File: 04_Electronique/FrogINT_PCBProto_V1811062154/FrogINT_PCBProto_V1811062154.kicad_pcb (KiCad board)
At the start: 2 copper layers, 75.8 x 75.8 mm, 38 parts, among them IC1 TTP223-BA6, J1 USB_B_Mini, J2 Conn_01x01_Female, J3 AVR-JTAG-10, Q1 PMV48XP, Q2 PMV48XP, U1 NCP1117-5.0_SOT223, U2 LP2985-3.3, U3 ATmega16U4RC-AU, Y1 16MHz

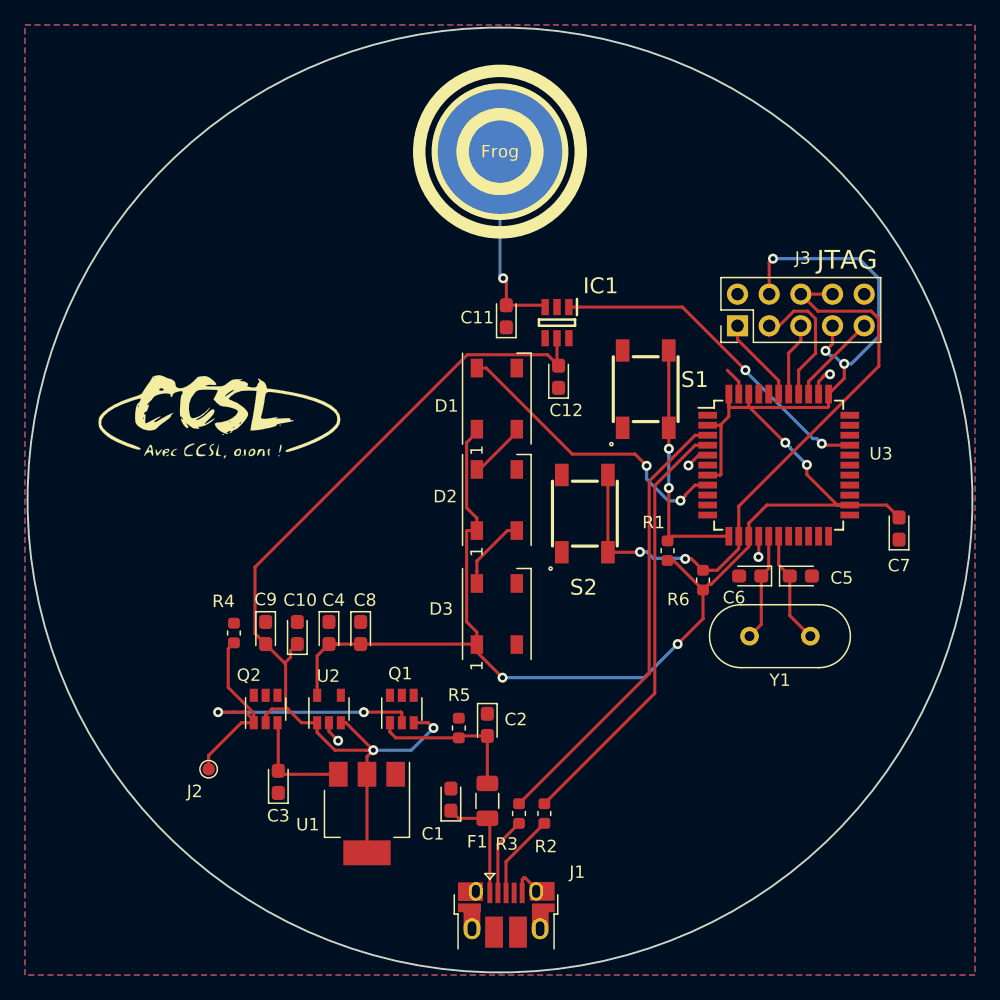
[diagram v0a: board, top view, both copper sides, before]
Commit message: Commit du 05/02/2019 :
Création d'une nouvelle forme de PCB,
Placement sommaire des composants,
Utilisation de Freerouting.jar pour effectuer une partie du routage.
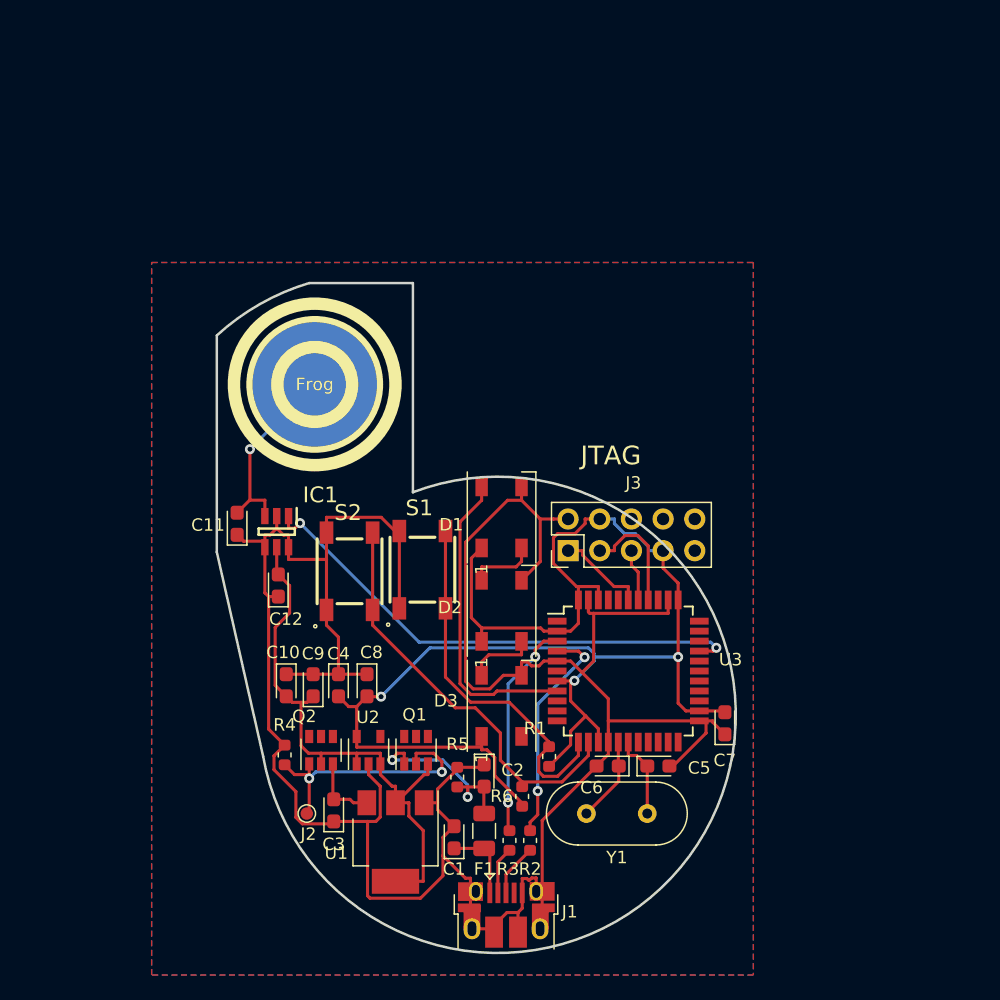
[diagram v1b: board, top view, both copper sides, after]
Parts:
- removed G***: LOGO, FTA_FrogINT_Library_Footprint_Package:Logo_CCSL_Silk
- removed G***: LOGO, FTA_FrogINT_Library_Footprint_Package:Logo_CCSL_Silk_Bottom
- removed G***: LOGO, FTA_FrogINT_Library_Footprint_Package:Logo_Thales_Silk_Bottom
- moved IC1 28.0 mm to (124.8, 100.8)
- moved C12 28.0 mm to (125.0, 105.2)
- moved C11 27.3 mm to (121.7, 100.2)
- moved TS1 23.9 mm to (127.9, 89.0)
- moved S1 23.0 mm to (136.5, 103.9)
- moved R6 22.6 mm to (144.5, 122.1)
- moved J3 22.6 mm to (148.2, 102.4)
- moved C7 21.0 mm to (160.8, 116.2)
- moved U3 20.4 mm to (153.0, 112.0)
- moved S2 19.4 mm to (130.7, 104.0)
- moved Y1 19.3 mm to (154.6, 123.4)
- moved C6 19.1 mm to (151.4, 119.6)
- moved C5 19.0 mm to (155.4, 119.6)
- moved R1 19.0 mm to (146.7, 118.9)
- moved R4 10.6 mm to (125.5, 118.7)
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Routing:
- net GND: track 12.6 -> 217.9 mm, vias 4 -> 0
- net +5V: track 79.0 -> 46.5 mm, vias 2 -> 0
- net +3V3: track 142.6 -> 120.1 mm, vias 7 -> 3
- net /D-: track 36.4 -> 17.5 mm, vias 0 -> 2
- net /reset: track 50.7 -> 33.5 mm, vias 2 -> 0
- net /D+: track 34.8 -> 18.1 mm, vias 0 -> 2
- net /Input_Int_Touch: track 27.2 -> 41.1 mm
- net /Vin: track 32.1 -> 21.2 mm
- net /Input_Interrupt: track 20.4 -> 30.0 mm, vias 2 -> 0
- net Net-(J3-Pad9): track 7.32 -> 0.00 mm
- net Net-(C3-Pad2): track 8.81 -> 5.63 mm
- net Net-(C1-Pad1): track 9.24 -> 6.17 mm
- net Net-(J3-Pad3): track 12.2 -> 9.29 mm
- net Net-(J1-Pad3): track 6.85 -> 4.22 mm
- net Net-(J1-Pad2): track 6.28 -> 3.80 mm
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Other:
- board size 75.8 x 75.8 mm -> 41.6 x 53.7 mm

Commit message: 12/02/2019 : Remplacement des gros boutons par des plus petits
Impact :
	Mise à jour du fichier Excel FrogINT_BOM_V03-Commit-22-01-2019_RFQ_RS.xlsx suite à la mise à jour de la BOM (Attention pour les chiffrage en cours)
	Création des fichiers sources mécaniques pour ce nouveau Switch_PTS810SJG250SMTRLFS
	Mise à jour des références des librairies (pointeur).
	Déplacement partiel de la librairie SamacSys_Parts directement dans la "racine" du projet (et non plus dans l'arborescence C: etc.)
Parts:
- S1, S2: value SKQGAKE010 -> PTS810SJG250SMTRLFS; footprint SamacSys_Parts:SKQGAKE010 -> SamacSys_Parts:PTS810SJG250SMTRLFS
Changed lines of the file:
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@@
   (page A4)
   (layers
-    (0 F.Cu signal)
-    (31 B.Cu signal)
+    (0 F.Cu signal hide)
+    (31 B.Cu signal hide)
     (32 B.Adhes user)
     (33 F.Adhes user)
@@
     (add_net /Cap-TouchSensor)
   )
+  (module SamacSys_Parts:PTS810SJG250SMTRLFS (layer F.Cu)
+    (at 136.525 103.886 90)
+    (descr pts810)
+    (tags Switch)
+    (attr smd)
+    (fp_text reference S1 (at -0.25 0 90) (layer F.SilkS)
+      (effects (font (size 1.27 1.27) (thickness 0.254)))
+    )
+    (fp_text value PTS810SJG250SMTRLFS (at -0.25 0 90) (layer F.SilkS) hide
+      (effects (font (size 1.27 1.27) (thickness 0.254)))
+    )
+    (fp_arc (start -3 -1.1) (end -3 -1) (angle 180) (layer F.SilkS) (width 0.2))
+    (fp_arc (start -3 -1.1) (end -3 -1.2) (angle 180) (layer F.SilkS) (width 0.2))
+    (fp_line (start -3 -1) (end -3 -1) (layer F.SilkS) (width 0.2))
+    (fp_line (start -3 -1.2) (end -3 -1.2) (layer F.SilkS) (width 0.2))
+    (fp_line (start -2.1 1.6) (end 2.075 1.6) (layer F.SilkS) (width 0.1))
+    (fp_line (start -2.1 -1.6) (end 2.075 -1.6) (layer F.SilkS) (width 0.1))
+    (fp_line (start -4.1 2.6) (end -4.1 -2.6) (layer Dwgs.User) (width 0.1))
+    (fp_line (start 3.6 2.6) (end -4.1 2.6) (layer Dwgs.User) (width 0.1))
+    (fp_line (start 3.6 -2.6) (end 3.6 2.6) (layer Dwgs.User) (width 0.1))
+    (fp_line (start -4.1 -2.6) (end 3.6 -2.6) (layer Dwgs.User) (width 0.1))
+    (fp_line (start -2.1 1.6) (end -2.1 -1.6) (layer Dwgs.User) (width 0.2))
+    (fp_line (start 2.1 1.6) (end -2.1 1.6) (layer Dwgs.User) (width 0.2))
+    (fp_line (start 2.1 -1.6) (end 2.1 1.6) (layer Dwgs.User) (width 0.2))
+    (fp_line (start -2.1 -1.6) (end 2.1 -1.6) (layer Dwgs.User) (width 0.2))
+    (pad 4 smd rect (at 2.075 1.075 180) (size 0.65 1.05) (layers F.Cu F.Paste F.Mask)
+      (net 22 /Input_Interrupt))
+    (pad 3 smd rect (at -2.075 1.075 180) (size 0.65 1.05) (layers F.Cu F.Paste F.Mask)
+      (net 22 /Input_Interrupt))
+    (pad 2 smd rect (at 2.075 -1.075 180) (size 0.65 1.05) (layers F.Cu F.Paste F.Mask)
+      (net 1 GND))
+    (pad 1 smd rect (at -2.075 -1.075 180) (size 0.65 1.05) (layers F.Cu F.Paste F.Mask)
+      (net 1 GND))
+    (model ${KIPRJMOD}/Library/PTS810SJG250SMTRLFS.step
+      (at (xyz 0 0 0))
+      (scale (xyz 1 1 1))
+      (rotate (xyz 0 0 0))
+    )
+  )
+  (module SamacSys_Parts:PTS810SJG250SMTRLFS (layer F.Cu)
+    (at 130.683 104.013 90)
+    (descr pts810)
+    (tags Switch)
+    (attr smd)
+    (fp_text reference S2 (at -0.25 0 90) (layer F.SilkS)
+      (effects (font (size 1.27 1.27) (thickness 0.254)))
+    )
+    (fp_text value PTS810SJG250SMTRLFS (at -0.25 0 90) (layer F.SilkS) hide
+      (effects (font (size 1.27 1.27) (thickness 0.254)))
+    )
+    (fp_line (start -2.1 -1.6) (end 2.1 -1.6) (layer Dwgs.User) (width 0.2))
+    (fp_line (start 2.1 -1.6) (end 2.1 1.6) (layer Dwgs.User) (width 0.2))
+    (fp_line (start 2.1 1.6) (end -2.1 1.6) (layer Dwgs.User) (width 0.2))
+    (fp_line (start -2.1 1.6) (end -2.1 -1.6) (layer Dwgs.User) (width 0.2))
+    (fp_line (start -4.1 -2.6) (end 3.6 -2.6) (layer Dwgs.User) (width 0.1))
+    (fp_line (start 3.6 -2.6) (end 3.6 2.6) (layer Dwgs.User) (width 0.1))
+    (fp_line (start 3.6 2.6) (end -4.1 2.6) (layer Dwgs.User) (width 0.1))
+    (fp_line (start -4.1 2.6) (end -4.1 -2.6) (layer Dwgs.User) (width 0.1))
+    (fp_line (start -2.1 -1.6) (end 2.075 -1.6) (layer F.SilkS) (width 0.1))
+    (fp_line (start -2.1 1.6) (end 2.075 1.6) (layer F.SilkS) (width 0.1))
+    (fp_line (start -3 -1.2) (end -3 -1.2) (layer F.SilkS) (width 0.2))
+    (fp_line (start -3 -1) (end -3 -1) (layer F.SilkS) (width 0.2))
+    (fp_arc (start -3 -1.1) (end -3 -1.2) (angle 180) (layer F.SilkS) (width 0.2))
+    (fp_arc (start -3 -1.1) (end -3 -1) (angle 180) (layer F.SilkS) (width 0.2))
+    (pad 1 smd rect (at -2.075 -1.075 180) (size 0.65 1.05) (layers F.Cu F.Paste F.Mask)
+      (net 1 GND))
+    (pad 2 smd rect (at 2.075 -1.075 180) (size 0.65 1.05) (layers F.Cu F.Paste F.Mask)
+      (net 1 GND))
+    (pad 3 smd rect (at -2.075 1.075 180) (size 0.65 1.05) (layers F.Cu F.Paste F.Mask)
+      (net 20 /reset))
+    (pad 4 smd rect (at 2.075 1.075 180) (size 0.65 1.05) (layers F.Cu F.Paste F.Mask)
+      (net 20 /reset))
+    (model ${KIPRJMOD}/Library/PTS810SJG250SMTRLFS.step
+      (at (xyz 0 0 0))
+      (scale (xyz 1 1 1))
+      (rotate (xyz 0 0 0))
+    )
+  )
   (module FTA_FrogINT_Library_Footprint_Package:CP_EIA-2012-12_Kemet-R (layer F.Cu)
     (at 139.065 125.349 90)
@@
       (net 47 /Input_Int_Touch))
   )
-  (module SamacSys_Parts:SKQGAKE010 (layer F.Cu)
-    (at 136.525 103.886 90)
-    (descr SKQGAKE010)
-    (tags Switch)
-    (attr smd)
-    (fp_text reference S1 (at 4.953 -0.254 180) (layer F.SilkS)
-      (effects (font (size 1.27 1.27) (thickness 0.254)))
-    )
-    (fp_text value SKQGAKE010 (at -0.37 -0.055 90) (layer F.SilkS) hide
-      (effects (font (size 1.27 1.27) (thickness 0.254)))
-    )
-    (fp_circle (center -4.411 -2.749) (end -4.47067 -2.749) (layer F.SilkS) (width 0.254))
-    (fp_line (start -2.6 -1) (end -2.6 1) (layer F.SilkS) (width 0.254))
-    (fp_line (start 2.6 -1) (end 2.6 1) (layer F.SilkS) (width 0.254))
-    (fp_line (start -2.6 2.6) (end 2.6 2.6) (layer F.SilkS) (width 0.254))
-    (fp_line (start -2.6 -2.6) (end 2.6 -2.6) (layer F.SilkS) (width 0.254))
-    (fp_line (start -2.6 2.6) (end -2.6 -2.6) (layer Dwgs.User) (width 0.254))
-    (fp_line (start 2.6 2.6) (end -2.6 2.6) (layer Dwgs.User) (width 0.254))
-    (fp_line (start 2.6 -2.6) (end 2.6 2.6) (layer Dwgs.User) (width 0.254))
-    (fp_line (start -2.6 -2.6) (end 2.6 -2.6) (layer Dwgs.User) (width 0.254))
-    (pad 4 smd rect (at 3.1 1.85 180) (size 1.1 1.8) (layers F.Cu F.Paste F.Mask)
-      (net 22 /Input_Interrupt))
-    (pad 3 smd rect (at -3.1 1.85 180) (size 1.1 1.8) (layers F.Cu F.Paste F.Mask)
-      (net 22 /Input_Interrupt))
-    (pad 2 smd rect (at 3.1 -1.85 180) (size 1.1 1.8) (layers F.Cu F.Paste F.Mask)
-      (net 1 GND))
-    (pad 1 smd rect (at -3.1 -1.85 180) (size 1.1 1.8) (layers F.Cu F.Paste F.Mask)
-      (net 1 GND))
-  )
-  (module SamacSys_Parts:SKQGAKE010 (layer F.Cu)
-    (at 130.683 104.013 90)
-    (descr SKQGAKE010)
-    (tags Switch)
-    (attr smd)
-    (fp_text reference S2 (at 4.699 -0.127 180) (layer F.SilkS)
-      (effects (font (size 1.27 1.27) (thickness 0.254)))
-    )
-    (fp_text value SKQGAKE010 (at -0.37 -0.055 90) (layer F.SilkS) hide
-      (effects (font (size 1.27 1.27) (thickness 0.254)))
-    )
-    (fp_circle (center -4.411 -2.749) (end -4.47067 -2.749) (layer F.SilkS) (width 0.254))
-    (fp_line (start -2.6 -1) (end -2.6 1) (layer F.SilkS) (width 0.254))
-    (fp_line (start 2.6 -1) (end 2.6 1) (layer F.SilkS) (width 0.254))
-    (fp_line (start -2.6 2.6) (end 2.6 2.6) (layer F.SilkS) (width 0.254))
-    (fp_line (start -2.6 -2.6) (end 2.6 -2.6) (layer F.SilkS) (width 0.254))
-    (fp_line (start -2.6 2.6) (end -2.6 -2.6) (layer Dwgs.User) (width 0.254))
-    (fp_line (start 2.6 2.6) (end -2.6 2.6) (layer Dwgs.User) (width 0.254))
-    (fp_line (start 2.6 -2.6) (end 2.6 2.6) (layer Dwgs.User) (width 0.254))
-    (fp_line (start -2.6 -2.6) (end 2.6 -2.6) (layer Dwgs.User) (width 0.254))
-    (pad 4 smd rect (at 3.1 1.85 180) (size 1.1 1.8) (layers F.Cu F.Paste F.Mask)
-      (net 20 /reset))
-    (pad 3 smd rect (at -3.1 1.85 180) (size 1.1 1.8) (layers F.Cu F.Paste F.Mask)
-      (net 20 /reset))
-    (pad 2 smd rect (at 3.1 -1.85 180) (size 1.1 1.8) (layers F.Cu F.Paste F.Mask)
-      (net 1 GND))
-    (pad 1 smd rect (at -3.1 -1.85 180) (size 1.1 1.8) (layers F.Cu F.Paste F.Mask)
-      (net 1 GND))
-  )
   (module TestPoint:TestPoint_Pad_D1.0mm (layer F.Cu)

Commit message: Modification mineur pour réaliser des exports graphiques uniquement.
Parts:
- added G***: LOGO, FTA_FrogINT_Library_Footprint_Package:Logo_Thales_Silk_Bottom, F.Cu at (141.9, 114.0)

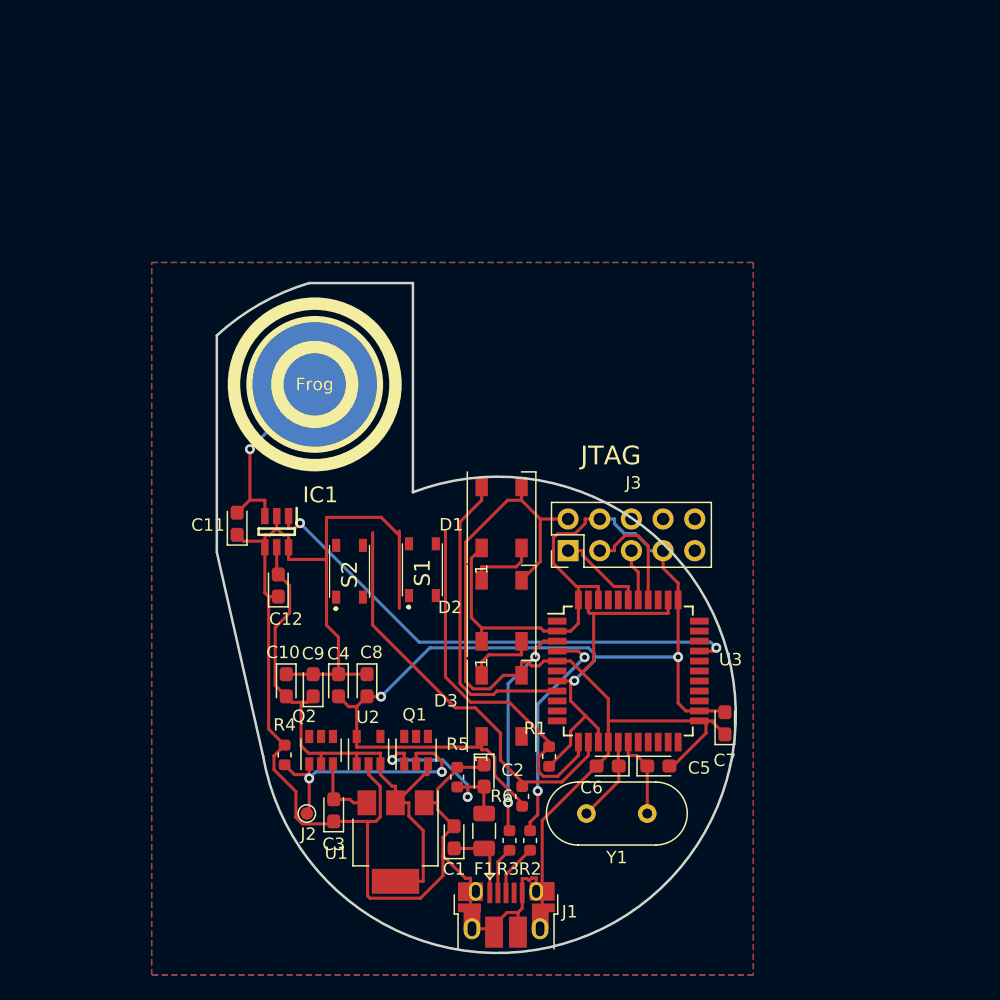
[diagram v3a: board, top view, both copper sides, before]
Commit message: Commit du 14/03/2019 :
   - Remplacement header JTAG 2.54 par un header au format 1.27 afin de réduire taille sur le PCB
   - Suppression des composants ainsi que du TouchPAD sur le PCB, au profit d'un simple connecteur header 2.54 ==> Permettra le raccordement directement des modules chinois
   - Modification de la librairie du connecteur USB 47642.
   - Modification du footprint du connecteur USB 47642 afin de tenir compte de l'aspect "Throughole".
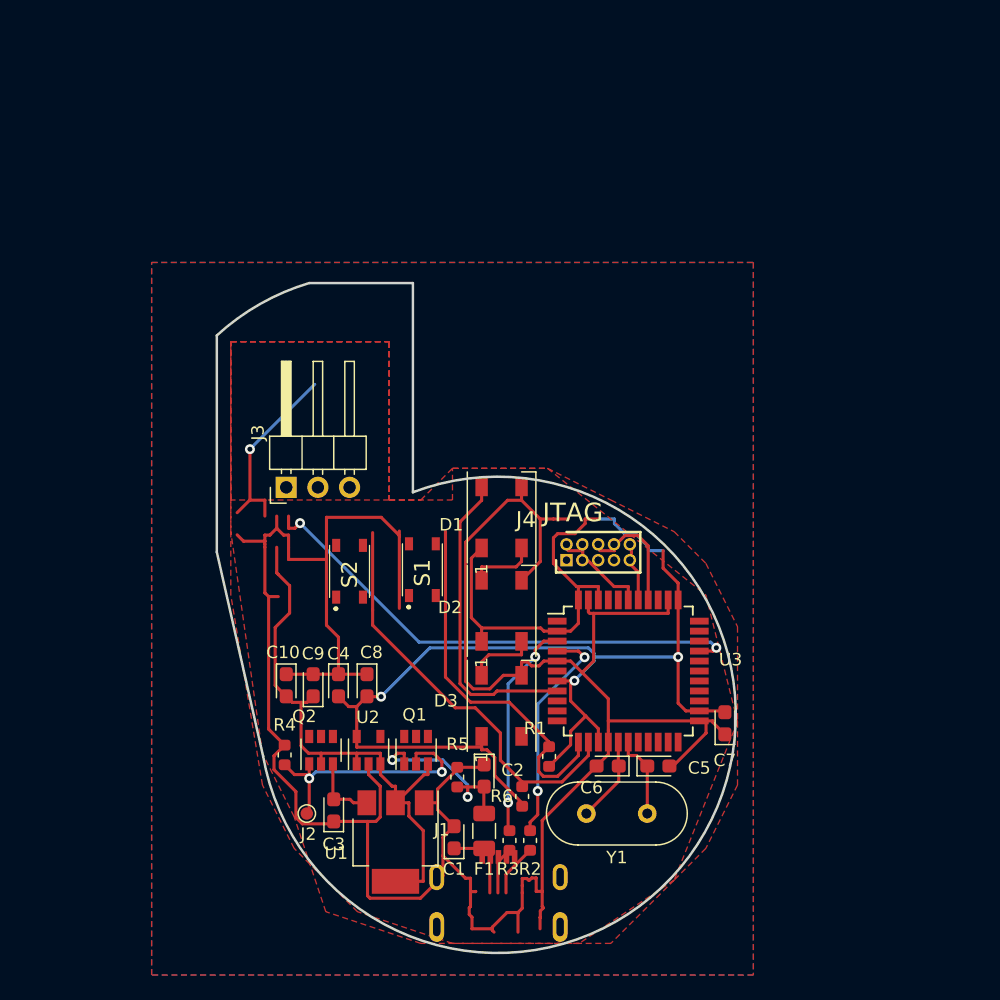
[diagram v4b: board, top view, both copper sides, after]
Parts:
- removed C11: 22pF, FTA_FrogINT_Library_Footprint_Package:CP_EIA-2012-12_Kemet-R
- removed C12: 100nF, FTA_FrogINT_Library_Footprint_Package:CP_EIA-2012-12_Kemet-R
- removed G***: LOGO, FTA_FrogINT_Library_Footprint_Package:Logo_Thales_Silk_Bottom
- removed IC1: TTP223-BA6, SamacSys_Parts:SOT95P285X126-6N
- removed TS1: TouchSense, FTA_FrogINT_Library_Footprint_Package:CapacitiveTouchSense_Bottom_10mm
- added J4: JTAG, FTA_FrogINT_Library_Footprint_Package:JTAG_HDRV10W41P127_2X5_676X325X510P, F.Cu at (148.1, 103.1)
- J1: footprint Connector_USB:USB_Micro-B_Amphenol_10103594-0001LF_Horizontal -> FTA_FrogINT_Library_Footprint_Package:47642-0001_Molex_USB
- J3: value AVR-JTAG-10 -> Conn_01x03; footprint FTA_FrogINT_Library_Footprint_Package:PinHeader_2x05_P2.54mm_Vertical -> Connector_PinHeader_2.54mm:PinHeader_1x03_P2.54mm_Horizontal
- moved J3 23.2 mm to (125.6, 97.3)
- moved J1 2.99 mm to (142.6, 134.5)
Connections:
- J3 pad 1: Net-(J3-Pad1) -> /Input_Int_Touch
- J3 pad 2: GND -> +3V3
- J3 pad 3: Net-(J3-Pad3) -> GND
- U3 pad 36: Net-(J3-Pad9) -> Net-(J4-Pad9)
- U3 pad 37: Net-(J3-Pad3) -> Net-(J4-Pad3)
- U3 pad 38: Net-(J3-Pad5) -> Net-(J4-Pad5)
- U3 pad 39: Net-(J3-Pad1) -> Net-(J4-Pad1)
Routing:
- net +3V3: track 120.1 -> 113.6 mm
- net GND: track 217.9 -> 224.4 mm
- net Net-(J4-Pad5): track 0.00 -> 4.18 mm
- net Net-(J3-Pad5): track 4.18 -> 0.00 mm
